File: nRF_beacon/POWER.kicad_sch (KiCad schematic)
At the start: 17 parts, among them U2 NPM1300-QEAA-R7

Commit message: Finished first schematic draft. Ready for layout
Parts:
- C14, C16, C23, C24, C25: footprint (none) -> Capacitor_SMD:C_0603_1608Metric_Pad1.08x0.95mm_HandSolder; MPN (none) -> KGM15CR51E106KT; Price (none) -> 5.09
- C15: footprint (none) -> Capacitor_SMD:C_0603_1608Metric_Pad1.08x0.95mm_HandSolder; MPN (none) -> GRM188Z71C225KE43D; Price (none) -> 1.6
- C22: value 100nF -> 0.1uF; footprint (none) -> Capacitor_SMD:C_0201_0603Metric_Pad0.64x0.40mm_HandSolder; MPN (none) -> KGM03BR51E104KH; Price (none) -> 1.39
- D1: footprint (none) -> Ekse:APGF1012GBRC07
- L5, L6: footprint (none) -> Ekse:INDC2016X100N; MPN (none) -> MLP2016V2R2MT0S1; Price (none) -> 2.19
- NT1, NT2: footprint (none) -> NetTie:NetTie-4_SMD_Pad0.5mm
- R3, R4: footprint (none) -> Resistor_SMD:R_0603_1608Metric_Pad0.98x0.95mm_HandSolder; MPN (none) -> CRCW060310K0FKEI; Price (none) -> 2.49
- R5, R6: value R_Small -> 150k; footprint (none) -> Resistor_SMD:R_0201_0603Metric_Pad0.64x0.40mm_HandSolder; MPN (none) -> CRCW0201150KFKED; Price (none) -> 2.10
- U2: MPN (none) -> NPM1300-QEAA-R7; Price (none) -> 15.31
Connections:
- net VDD_nRF: now also D1.4 (A); no longer D1.1 (A)
- net at U2.27 (LED2): now also D1.1 (RK); no longer D1.4 (RK)
- net NTC: no longer names the net of U2.18 (NTC)
- net PVSS1: no longer names the net of C14.2, NT2.1, U2.2 (PVSS1)
- net PVSS1: no longer C23.2
- net PVSS2: no longer names the net of C16.2, NT1.1, U2.6 (PVSS2)
- net PVSS2: no longer C24.2
- no-connect marks 16 -> 15
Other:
- note added: "Dependent on bus speed and parasitic capacitances"

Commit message: Began matching network layout
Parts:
- C14, C15, C16, C23, C24, C25: footprint Capacitor_SMD:C_0603_1608Metric_Pad1.08x0.95mm_HandSolder -> Capacitor_SMD:C_0603_1608Metric
- C22: footprint Capacitor_SMD:C_0201_0603Metric_Pad0.64x0.40mm_HandSolder -> Capacitor_SMD:C_0201_0603Metric
- R3, R4: footprint Resistor_SMD:R_0603_1608Metric_Pad0.98x0.95mm_HandSolder -> Resistor_SMD:R_0603_1608Metric
- R5, R6: footprint Resistor_SMD:R_0201_0603Metric_Pad0.64x0.40mm_HandSolder -> Resistor_SMD:R_0201_0603Metric
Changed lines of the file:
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@@
 			)
 		)
-		(property "Footprint" "Capacitor_SMD:C_0603_1608Metric_Pad1.08x0.95mm_HandSolder"
+		(property "Footprint" "Capacitor_SMD:C_0603_1608Metric"
 			(at 195.58 87.63 0)
 			(effects
@@
 			)
 		)
-		(property "Footprint" "Resistor_SMD:R_0603_1608Metric_Pad0.98x0.95mm_HandSolder"
+		(property "Footprint" "Resistor_SMD:R_0603_1608Metric"
 			(at 106.68 144.78 0)
 			(effects
@@
 			)
 		)
-		(property "Footprint" "Capacitor_SMD:C_0603_1608Metric_Pad1.08x0.95mm_HandSolder"
+		(property "Footprint" "Capacitor_SMD:C_0603_1608Metric"
 			(at 101.6 85.09 0)
 			(effects
@@
 			)
 		)
-		(property "Footprint" "Capacitor_SMD:C_0201_0603Metric_Pad0.64x0.40mm_HandSolder"
+		(property "Footprint" "Capacitor_SMD:C_0201_0603Metric"
 			(at 82.55 154.94 0)
 			(effects
@@
 			)
 		)
-		(property "Footprint" "Resistor_SMD:R_0201_0603Metric_Pad0.64x0.40mm_HandSolder"
+		(property "Footprint" "Resistor_SMD:R_0201_0603Metric"
 			(at 90.17 127 0)
 			(effects
@@
 			)
 		)
-		(property "Footprint" "Capacitor_SMD:C_0603_1608Metric_Pad1.08x0.95mm_HandSolder"
+		(property "Footprint" "Capacitor_SMD:C_0603_1608Metric"
 			(at 186.69 67.31 0)
 			(effects
@@
 			)
 		)
-		(property "Footprint" "Capacitor_SMD:C_0603_1608Metric_Pad1.08x0.95mm_HandSolder"
+		(property "Footprint" "Capacitor_SMD:C_0603_1608Metric"
 			(at 204.47 67.31 0)
 			(effects
@@
 			)
 		)
-		(property "Footprint" "Resistor_SMD:R_0201_0603Metric_Pad0.64x0.40mm_HandSolder"
+		(property "Footprint" "Resistor_SMD:R_0201_0603Metric"
 			(at 104.14 127 0)
 			(effects
@@
 			)
 		)
-		(property "Footprint" "Capacitor_SMD:C_0603_1608Metric_Pad1.08x0.95mm_HandSolder"
+		(property "Footprint" "Capacitor_SMD:C_0603_1608Metric"
 			(at 195.58 110.49 0)
 			(effects
@@
 			)
 		)
-		(property "Footprint" "Capacitor_SMD:C_0603_1608Metric_Pad1.08x0.95mm_HandSolder"
+		(property "Footprint" "Capacitor_SMD:C_0603_1608Metric"
 			(at 195.58 67.31 0)
 			(effects
@@
 			)
 		)
-		(property "Footprint" "Resistor_SMD:R_0603_1608Metric_Pad0.98x0.95mm_HandSolder"
+		(property "Footprint" "Resistor_SMD:R_0603_1608Metric"
 			(at 115.57 144.78 0)
 			(effects

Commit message: Added most of the components to nRF54 typical application layout
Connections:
- net Earth renamed GND
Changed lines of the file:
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@@
 			)
 		)
-		(property "Value" "Earth"
+		(property "Value" "GND"
 			(at 204.47 76.2 0)
 			(effects
@@
 			)
 		)
-		(property "Description" "Power symbol creates a global label with name \"Earth\""
+		(property "Description" "Power symbol creates a global label with name \"GND\""
 			(at 204.47 71.12 0)
 			(effects
@@
 			)
 		)
-		(property "Value" "Earth"
+		(property "Value" "GND"
 			(at 217.17 101.6 0)
 			(effects
@@
 			)
 		)
-		(property "Description" "Power symbol creates a global label with name \"Earth\""
+		(property "Description" "Power symbol creates a global label with name \"GND\""
 			(at 217.17 96.52 0)
 			(effects
@@
 			)
 		)
-		(property "Value" "Earth"
+		(property "Value" "GND"
 			(at 101.6 97.79 0)
 			(effects
@@
 			)
 		)
-		(property "Description" "Power symbol creates a global label with name \"Earth\""
+		(property "Description" "Power symbol creates a global label with name \"GND\""
 			(at 101.6 92.71 0)
 			(effects
@@
 			)
 		)
-		(property "Value" "Earth"
+		(property "Value" "GND"
 			(at 90.17 135.89 0)
 			(effects
@@
 			)
 		)
-		(property "Description" "Power symbol creates a global label with name \"Earth\""
+		(property "Description" "Power symbol creates a global label with name \"GND\""
 			(at 90.17 130.81 0)
 			(effects
@@
 			)
 		)
-		(property "Value" "Earth"
+		(property "Value" "GND"
 			(at 82.55 165.1 0)
 			(effects
@@
 			)
 		)
-		(property "Description" "Power symbol creates a global label with name \"Earth\""
+		(property "Description" "Power symbol creates a global label with name \"GND\""
 			(at 82.55 160.02 0)
 			(effects
@@
 			)
 		)
-		(property "Value" "Earth"
+		(property "Value" "GND"
 			(at 184.15 162.56 0)
 			(effects
@@
 			)
 		)
-		(property "Description" "Power symbol creates a global label with name \"Earth\""
+		(property "Description" "Power symbol creates a global label with name \"GND\""
 			(at 184.15 157.48 0)
 			(effects
@@
 			)
 		)
-		(property "Value" "Earth"
+		(property "Value" "GND"
 			(at 104.14 135.89 0)
 			(effects
@@
 			)
 		)
-		(property "Description" "Power symbol creates a global label with name \"Earth\""
+		(property "Description" "Power symbol creates a global label with name \"GND\""
 			(at 104.14 130.81 0)
 			(effects
@@
 			)
 		)
-		(property "Value" "Earth"
+		(property "Value" "GND"
 			(at 215.9 124.46 0)
 			(effects
@@
 			)
 		)
-		(property "Description" "Power symbol creates a global label with name \"Earth\""
+		(property "Description" "Power symbol creates a global label with name \"GND\""
 			(at 215.9 119.38 0)
 			(effects

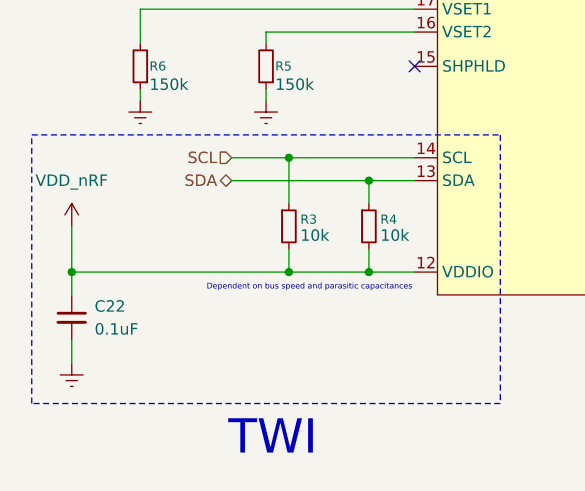
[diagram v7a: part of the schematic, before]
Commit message: Added transmission line, and new folder for report screenshots
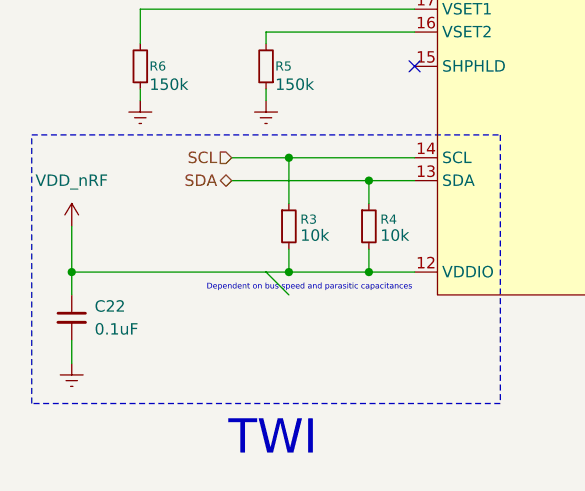
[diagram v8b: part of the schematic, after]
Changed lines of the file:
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@@
 		(at 120.65 127)
 	)
+	(bus_entry
+		(at 104.14 149.86)
+		(size 2.54 2.54)
+		(stroke
+			(width 0)
+			(type default)
+		)
+	)
 	(wire
 		(pts
@@
 	(wire
 		(pts
+			(xy 104.14 149.86) (xy 82.55 149.86)
+		)
+		(stroke
+			(width 0)
+			(type default)
+		)
+	)
+	(wire
+		(pts
 			(xy 182.88 83.82) (xy 182.88 85.09)
 		)
@@
 	(wire
 		(pts
-			(xy 106.68 149.86) (xy 82.55 149.86)
-		)
-		(stroke
+			(xy 106.68 149.86) (xy 104.14 149.86)
+		)
+		(stroke
